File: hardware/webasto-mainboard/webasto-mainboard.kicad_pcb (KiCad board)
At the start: 4 copper layers, 86.8 x 76 mm, 94 parts, among them J1 Console FTDI, J2 DEBUG, J3 2-pole connector, Q1 DMG2301L, Q10 DMG2301L, Q11 SSM3J374R, Q12 2N7002, Q13 SUD50P04-08, Q14 SUD50P04-08, Q15 SUD50P04-08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

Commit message: Added board sense, got FSM running, debugging
- Have FSM and global timer running in Core1, and the sensor stuff in
  Core0
- centralized the feedback to FSM, and made it wait until the FSM is
  initialized
- actually START and initialize the FSM correctly
- added in copious logging on state transitions, events
- debugged the global timer (which currently gets a tick every 10ms)
- debugged the internal temperature sensor:  it's 3.3V Vref when there's
  nothing external feeding into it.
- got the FRAM initialization in there, of course, no device yet.
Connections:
- U2 pad 29: unconnected-(U2-Pad29) -> GND

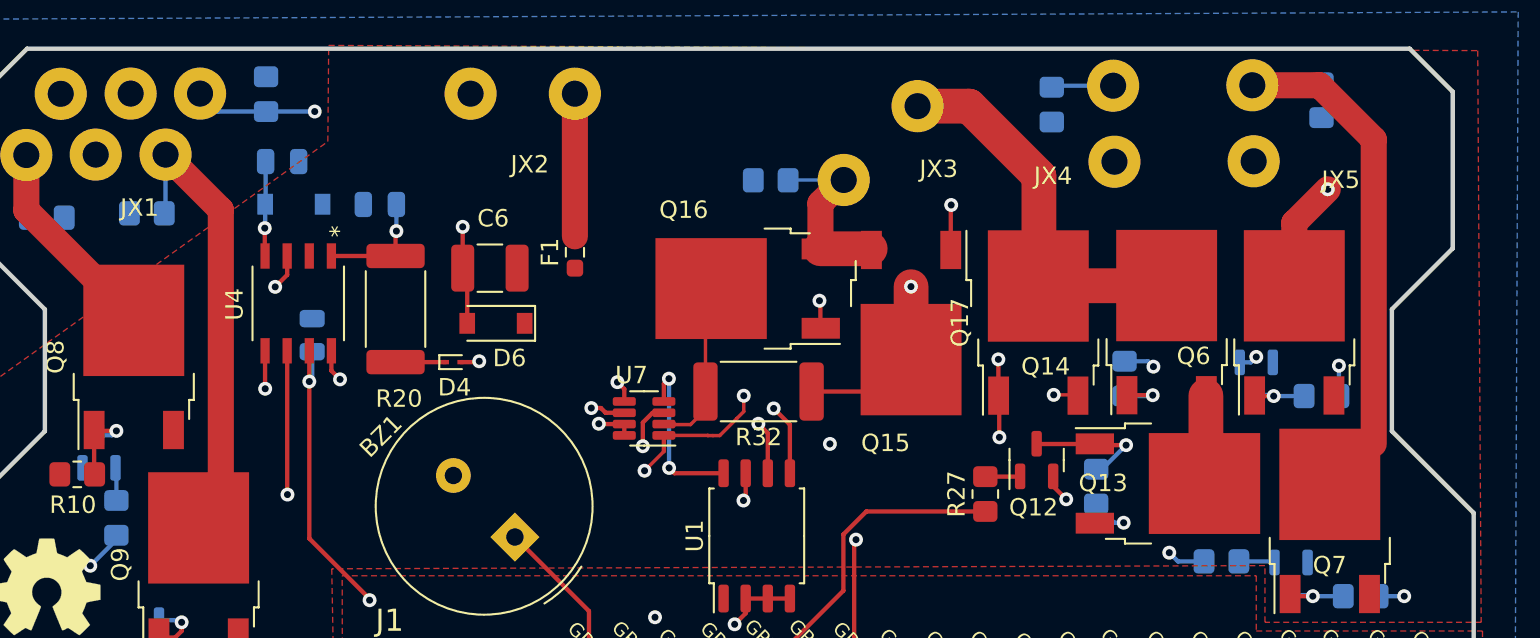
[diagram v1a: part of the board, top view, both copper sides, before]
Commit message: Added snubbing diodes on all the inputs
- back EMF from relays... I forgot...  so reverse biased diodes from
  GND to signal and from signal to +12V.
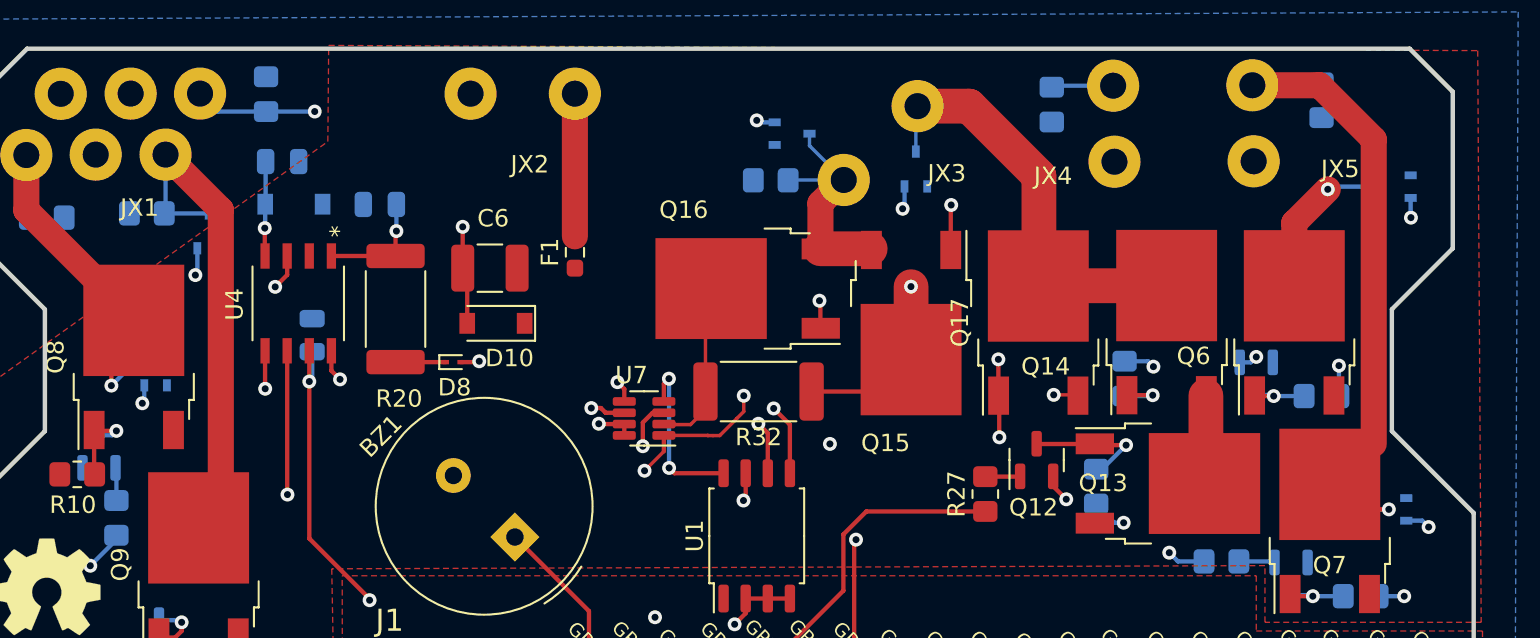
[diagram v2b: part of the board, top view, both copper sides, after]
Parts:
- added D12: BAT54SW, Package_TO_SOT_SMD:SOT-323_SC-70, B.Cu at (147.8, 58.4)
- added D13: BAT54SW, Package_TO_SOT_SMD:SOT-323_SC-70, B.Cu at (154.9, 60.5)
- added D3: BAT54SW, Package_TO_SOT_SMD:SOT-323_SC-70, B.Cu at (182.4, 61.5)
- added D4: BAT54SW, Package_TO_SOT_SMD:SOT-323_SC-70, B.Cu at (111.3, 71.9)
- added D5: BAT54SW, Package_TO_SOT_SMD:SOT-323_SC-70, B.Cu at (114.3, 64.0)
- added D6: BAT54SW, Package_TO_SOT_SMD:SOT-323_SC-70, B.Cu at (182.1, 80.0)
- U3: value LM4040DBZ-2.0 -> LM4040DIM3-3.0
- renumbered D6 to D10, D7 to D11, D3 to D7, D4 to D8, D5 to D9
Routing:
- net FuelPump: track 15.7 -> 23.4 mm, vias 0 -> 1
- net +12V: track 21.3 -> 28.9 mm, vias 7 -> 13
- net CirculationPump: track 33.3 -> 38.3 mm, vias 0 -> 1
- net GlowPlug-: track 10.6 -> 14.1 mm
- net CombustionFan: track 28.3 -> 31.1 mm
- net GlowPlug+: track 22.3 -> 24.9 mm
- net VehicleFanRelay: track 26.7 -> 29.3 mm
